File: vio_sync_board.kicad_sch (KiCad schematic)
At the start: 3 parts, among them IC1 Pololu 2595, U1 Pololu D24V5F1

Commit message: layout
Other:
- removed sheet testing
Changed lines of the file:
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@@
-		)
-	)
-	(sheet
-		(at 140.97 17.78)
-		(size 138.43 106.68)
-		(exclude_from_sim no)
-		(in_bom yes)
-		(on_board yes)
-		(dnp no)
-		(fields_autoplaced yes)
-		(stroke
-			(width 0.1524)
-			(type solid)
-		)
-		(fill
-			(color 0 0 0 0.0000)
-		)
-		(property "Sheetname" "testing"
-			(at 140.97 17.0684 0)
-			(effects
-				(font
-					(size 1.27 1.27)
-				)
-				(justify left bottom)
-			)
-		)
-		(property "Sheetfile" "testing.kicad_sch"
-			(at 140.97 125.0446 0)
-			(effects
-				(font
-					(size 1.27 1.27)
-				)
-				(justify left top)
-			)
-		)
-		(instances
-			(project "vio_sync_board"
-				(path "/a602f21e-3630-4741-8b13-b35321203336"
-					(page "2")
-				)
-			)
 		)
 	)

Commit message: update 1.8v dc convert footprint
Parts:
- IC1: footprint 2595 -> pololu_2595:2595
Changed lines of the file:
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@@
 			)
 		)
-		(property "Footprint" "2595"
+		(property "Footprint" "pololu_2595:2595"
 			(at 128.27 160.96 0)
 			(effects

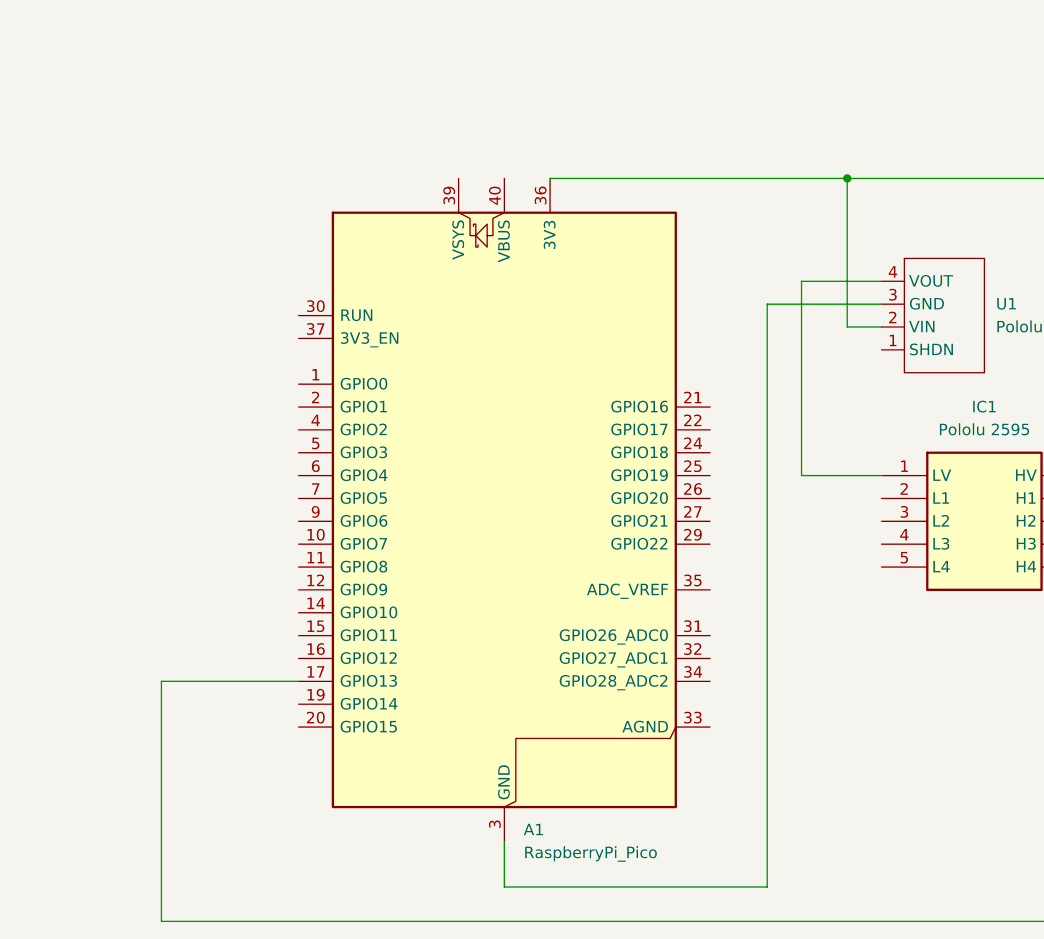
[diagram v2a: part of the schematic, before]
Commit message: add connector
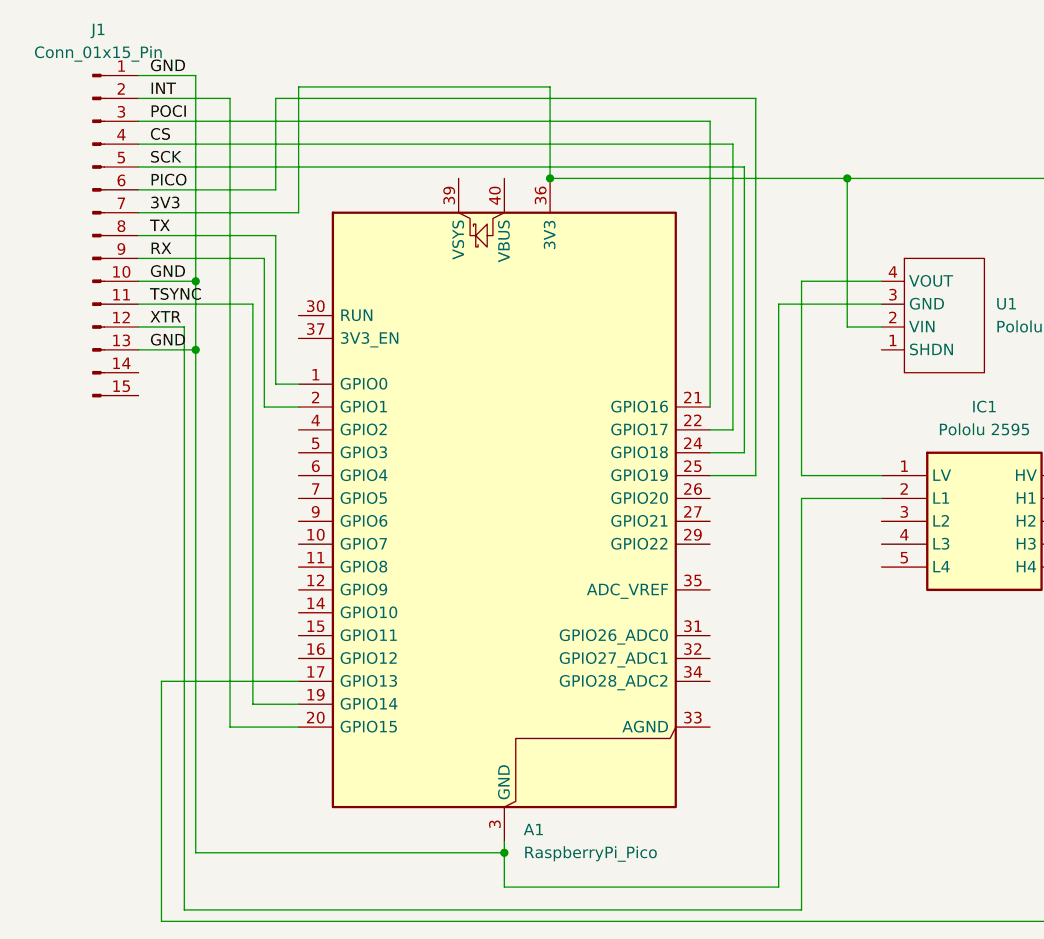
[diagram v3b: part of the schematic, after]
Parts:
- added J1: Conn_01x15_Pin, Connector_PinHeader_2.54mm:PinHeader_1x01_P2.54mm_Vertical, symbol Connector:Conn_01x15_Pin
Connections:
- net TX: now reaches A1.1 (GPIO0)
- net TX: now also J1.8 (Pin_8)
- net GND: now reaches A1.13 (GND), A1.18 (GND), A1.23 (GND), A1.28 (GND), A1.3 (GND), A1.38 (GND), A1.8 (GND), U1.3 (GND)
- net GND: now also J1.1 (Pin_1), J1.10 (Pin_10), J1.13 (Pin_13)
- net TSYNC: now reaches A1.19 (GPIO14)
- net TSYNC: now also J1.11 (Pin_11)
- net RX: now reaches A1.2 (GPIO1)
- net RX: now also J1.9 (Pin_9)
- net INT: now reaches A1.20 (GPIO15)
- net INT: now also J1.2 (Pin_2)
- net POCI: now reaches A1.21 (GPIO16)
- net POCI: now also J1.3 (Pin_3)
- net CS: now reaches A1.22 (GPIO17)
- net CS: now also J1.4 (Pin_4)
- net SCK: now reaches A1.24 (GPIO18)
- net SCK: now also J1.5 (Pin_5)
- net PICO: now reaches A1.25 (GPIO19)
- net PICO: now also J1.6 (Pin_6)
- net 3V3: now reaches A1.36 (3V3), IC1.6 (HV), U1.2 (VIN)
- net 3V3: now also J1.7 (Pin_7)
- net XTR: now reaches IC1.2 (L1)
- net XTR: now also J1.12 (Pin_12)

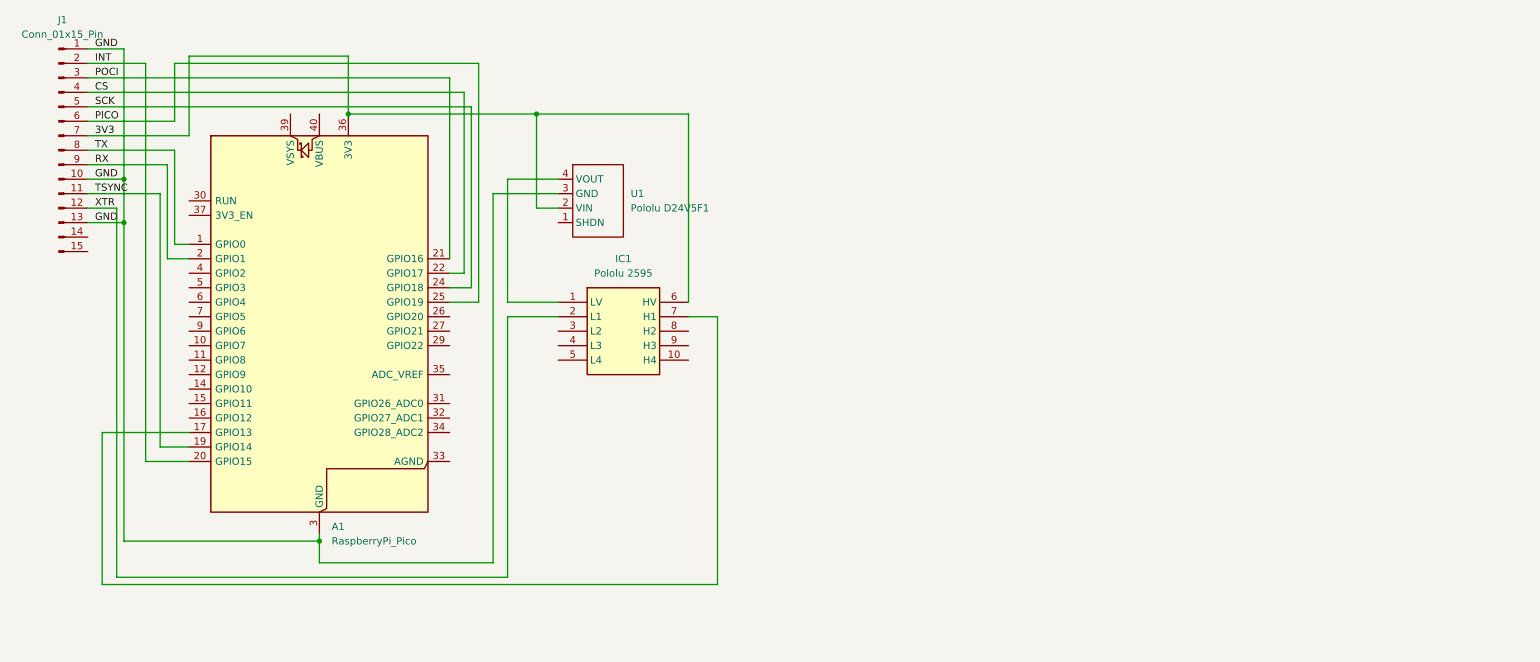
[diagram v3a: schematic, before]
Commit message: replace pololu dc converter and logic lv shifter
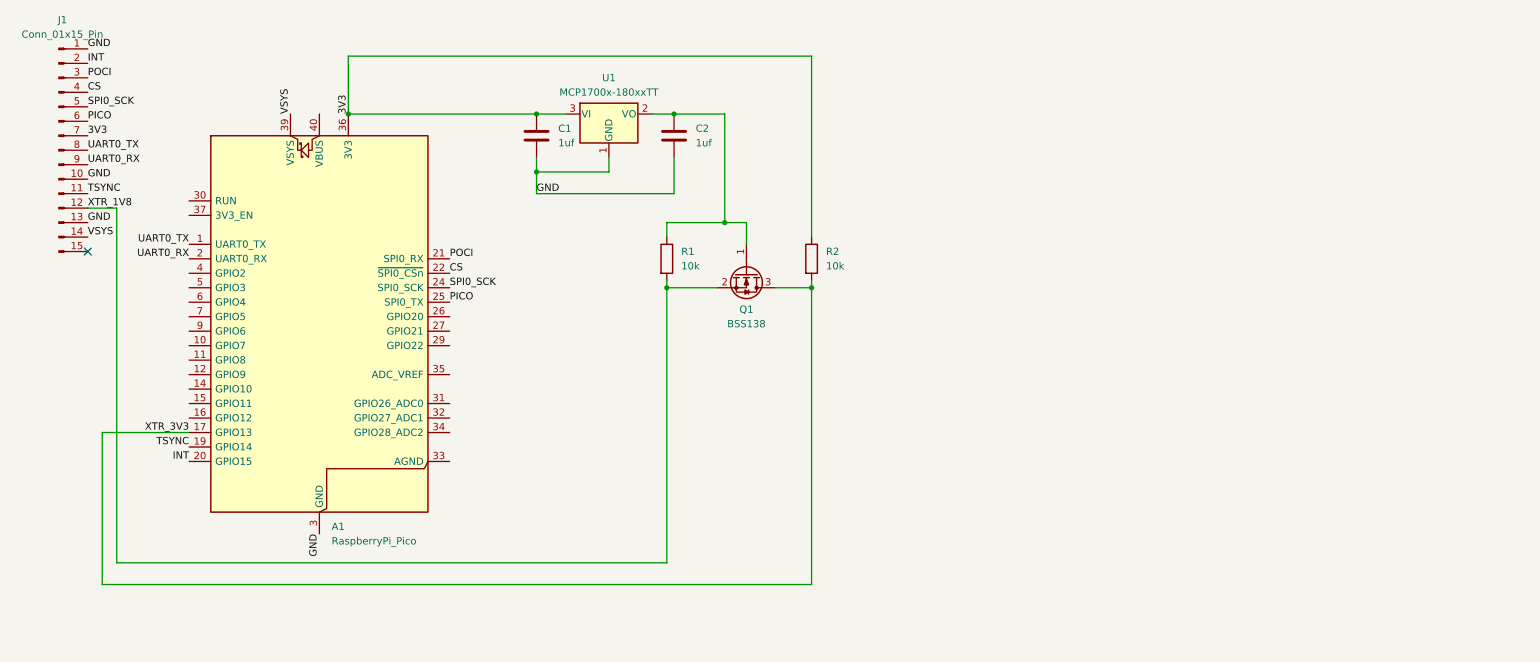
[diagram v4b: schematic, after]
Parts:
- removed IC1: Pololu 2595, pololu_2595:2595, symbol 2595:2595
- removed U1: Pololu D24V5F1, pololu_2840:D24V5F1, symbol pololu_2840:D24V5F1
- added C1, C2: 1uf, symbol Device:C
- added Q1: BSS138, Package_TO_SOT_SMD:SOT-23, symbol Transistor_FET:BSS138
- added R1, R2: 10k, symbol Device:R
- added U1: MCP1700x-180xxTT, Package_TO_SOT_SMD:SOT-23, symbol Regulator_Linear:MCP1700x-180xxTT
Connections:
- net 3V3: now also C1.1, R2.1, U1.3 (VI)
- net GND: now also C1.2, C2.2, U1.1 (GND)
- net XTR_3V3: now reaches A1.17 (GPIO13)
- net XTR_3V3: now also Q1.3 (D), R2.2
- net VSYS: now reaches A1.39 (VSYS)
- net VSYS: now also J1.14 (Pin_14)
- net RX renamed UART0_RX
- net SCK renamed SPI0_SCK
- net TX renamed UART0_TX
- net XTR renamed XTR_1V8
- net XTR_1V8: now also Q1.2 (S), R1.2
- new net: C2.1, Q1.1 (G), R1.1, U1.2 (VO)
- no-connect marks 0 -> 1

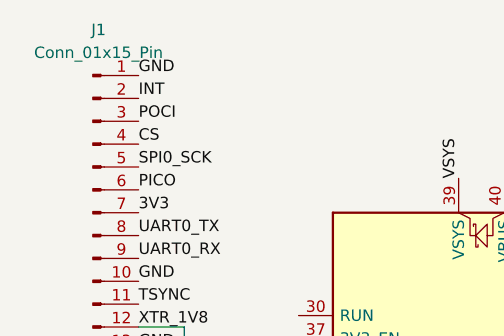
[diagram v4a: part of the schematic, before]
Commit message: resistor and capacitor footprint
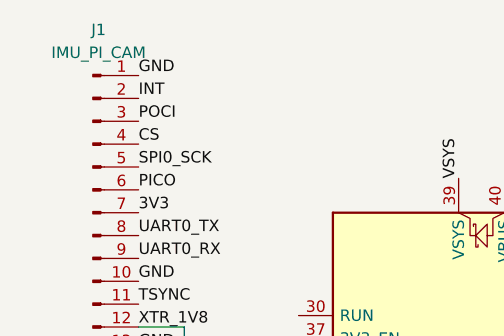
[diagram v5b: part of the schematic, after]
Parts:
- C1, C2: footprint (none) -> Capacitor_SMD:C_0805_2012Metric
- J1: value Conn_01x15_Pin -> IMU_PI_CAM
- R1, R2: footprint (none) -> Resistor_SMD:R_0805_2012Metric
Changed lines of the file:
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@@
 			)
 		)
-		(property "Footprint" ""
+		(property "Footprint" "Capacitor_SMD:C_0805_2012Metric"
 			(at 106.3752 40.64 0)
 			(effects
@@
 			)
 		)
-		(property "Footprint" ""
+		(property "Footprint" "Capacitor_SMD:C_0805_2012Metric"
 			(at 130.5052 40.64 0)
 			(effects
@@
 			)
 		)
-		(property "Footprint" ""
+		(property "Footprint" "Resistor_SMD:R_0805_2012Metric"
 			(at 126.492 58.42 90)
 			(effects
@@
 			)
 		)
-		(property "Value" "Conn_01x15_Pin"
+		(property "Value" "IMU_PI_CAM"
 			(at 22.225 19.05 0)
 			(effects
@@
 			)
 		)
-		(property "Footprint" ""
+		(property "Footprint" "Resistor_SMD:R_0805_2012Metric"
 			(at 151.892 58.42 90)
 			(effects

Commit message: fix connector footprint
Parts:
- J1: footprint Connector_PinHeader_2.54mm:PinHeader_1x01_P2.54mm_Vertical -> Connector_PinHeader_2.54mm:PinHeader_1x15_P2.54mm_Vertical
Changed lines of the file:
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@@
 			)
 		)
-		(property "Footprint" "Connector_PinHeader_2.54mm:PinHeader_1x01_P2.54mm_Vertical"
+		(property "Footprint" "Connector_PinHeader_2.54mm:PinHeader_1x15_P2.54mm_Vertical"
 			(at 21.59 39.37 0)
 			(effects

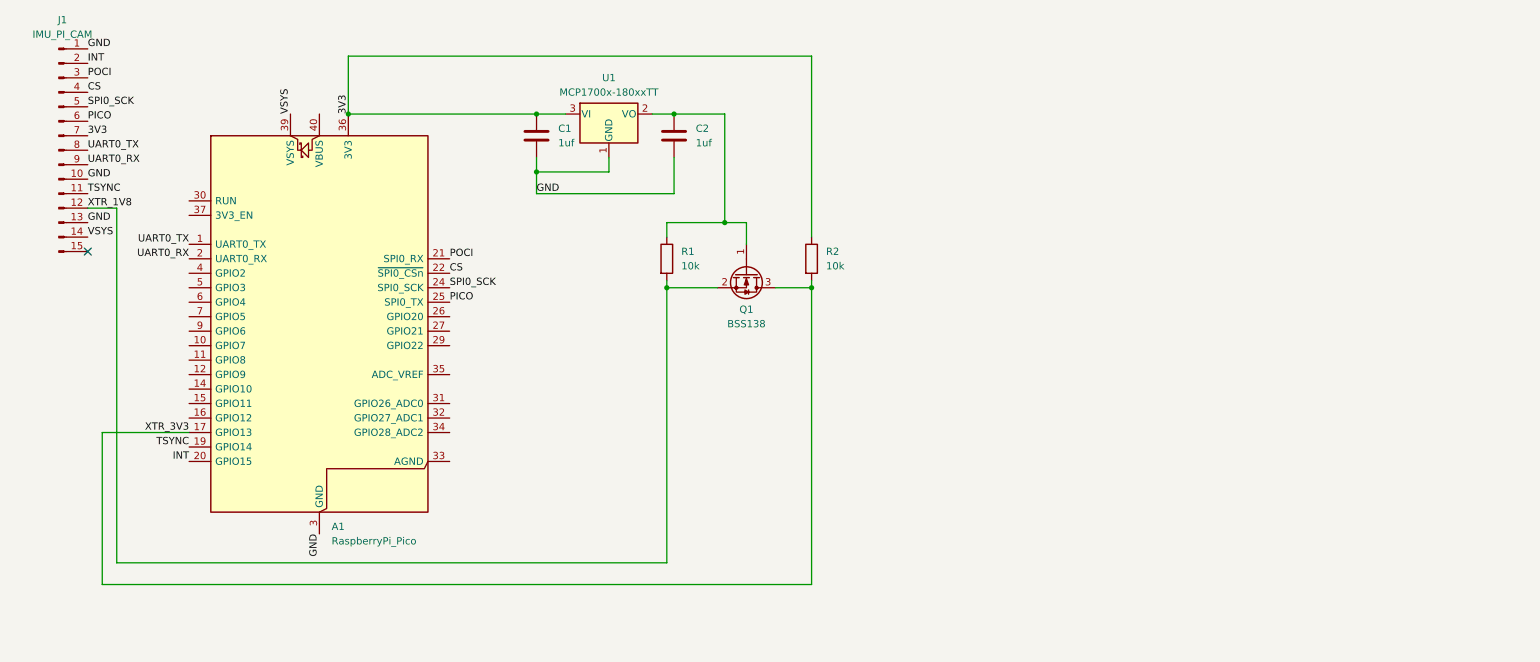
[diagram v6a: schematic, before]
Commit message: refine pin header
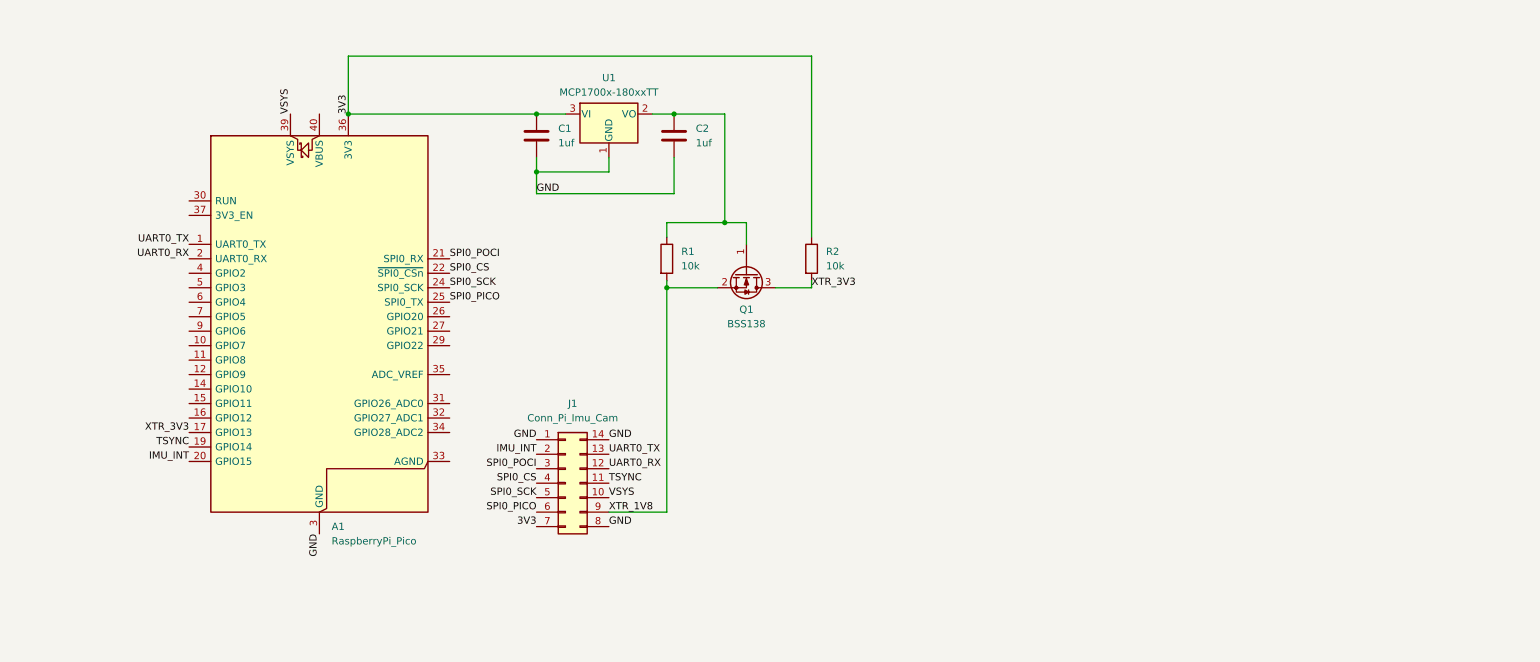
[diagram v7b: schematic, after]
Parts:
- removed J1: IMU_PI_CAM, Connector_PinHeader_2.54mm:PinHeader_1x15_P2.54mm_Vertical, symbol Connector:Conn_01x15_Pin
- added J1: Conn_Pi_Imu_Cam, Connector_PinHeader_2.54mm:PinHeader_2x07_P2.54mm_Vertical, symbol Connector_Generic:Conn_02x07_Counter_Clockwise
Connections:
- net 3V3: now also J1.7 (Pin_7)
- net GND: now also J1.1 (Pin_1), J1.14 (Pin_14), J1.8 (Pin_8)
- net SPI0_SCK: now also J1.5 (Pin_5)
- net TSYNC: now also J1.11 (Pin_11)
- net UART0_RX: now also J1.12 (Pin_12)
- net UART0_TX: now also J1.13 (Pin_13)
- net VSYS: now also J1.10 (Pin_10)
- net XTR_1V8: now also J1.9 (Pin_9)
- net CS renamed SPI0_CS
- net SPI0_CS: now also J1.4 (Pin_4)
- net INT renamed IMU_INT
- net IMU_INT: now also J1.2 (Pin_2)
- net PICO renamed SPI0_PICO
- net SPI0_PICO: now also J1.6 (Pin_6)
- net POCI renamed SPI0_POCI
- net SPI0_POCI: now also J1.3 (Pin_3)
- no-connect marks 1 -> 0

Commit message: layout
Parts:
- removed J1: Conn_Pi_Imu_Cam, Connector_PinHeader_2.54mm:PinHeader_2x07_P2.54mm_Vertical, symbol Connector_Generic:Conn_02x07_Counter_Clockwise
- added J1: Conn_IMU_Pi_Cam, Connector_PinHeader_2.54mm:PinHeader_2x07_P2.54mm_Vertical, symbol Connector_Generic:Conn_02x07_Odd_Even
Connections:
- net 3V3: now also J1.1 (Pin_1)
- net GND: now also J1.14 (Pin_14), J1.2 (Pin_2), J1.7 (Pin_7)
- net IMU_INT: now also J1.13 (Pin_13)
- net SPI0_CS: now also J1.9 (Pin_9)
- net SPI0_PICO: now also J1.3 (Pin_3)
- net SPI0_POCI: now also J1.11 (Pin_11)
- net SPI0_SCK: now also J1.5 (Pin_5)
- net TSYNC: now also J1.8 (Pin_8)
- net UART0_RX: now also J1.6 (Pin_6)
- net UART0_TX: now also J1.4 (Pin_4)
- net VSYS: now also J1.10 (Pin_10)
- net XTR_1V8: now also J1.12 (Pin_12)
